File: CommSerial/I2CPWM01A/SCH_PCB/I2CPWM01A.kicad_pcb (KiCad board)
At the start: 2 copper layers, 30 x 40.1 mm, 45 parts, among them J1 CONN1_2, J10 JUMP2_2x1, J11 JUMP2_2x1, J12 JUMP2_2x1, J13 JUMP2_2x1, J14 JUMP_2x1, J15 JUMP_2x1, J16 JUMP_2x1, J17 JUMP_2x1, J18 JUMP_2x1, J19 JUMP_2x1, J2 CONN1_2, J20 JUMP_2x1, J21 JUMP_2x1, J3 JUMP_3X2, J4 JUMP_5X2, J5 JUMP_2x1, J6 JUMP2_2x1, J7 JUMP2_2x1, J8 JUMP2_2x1, J9 JUMP2_2x1, P1 _, P2 _, P3 _, P4 _, U1 PCA9531

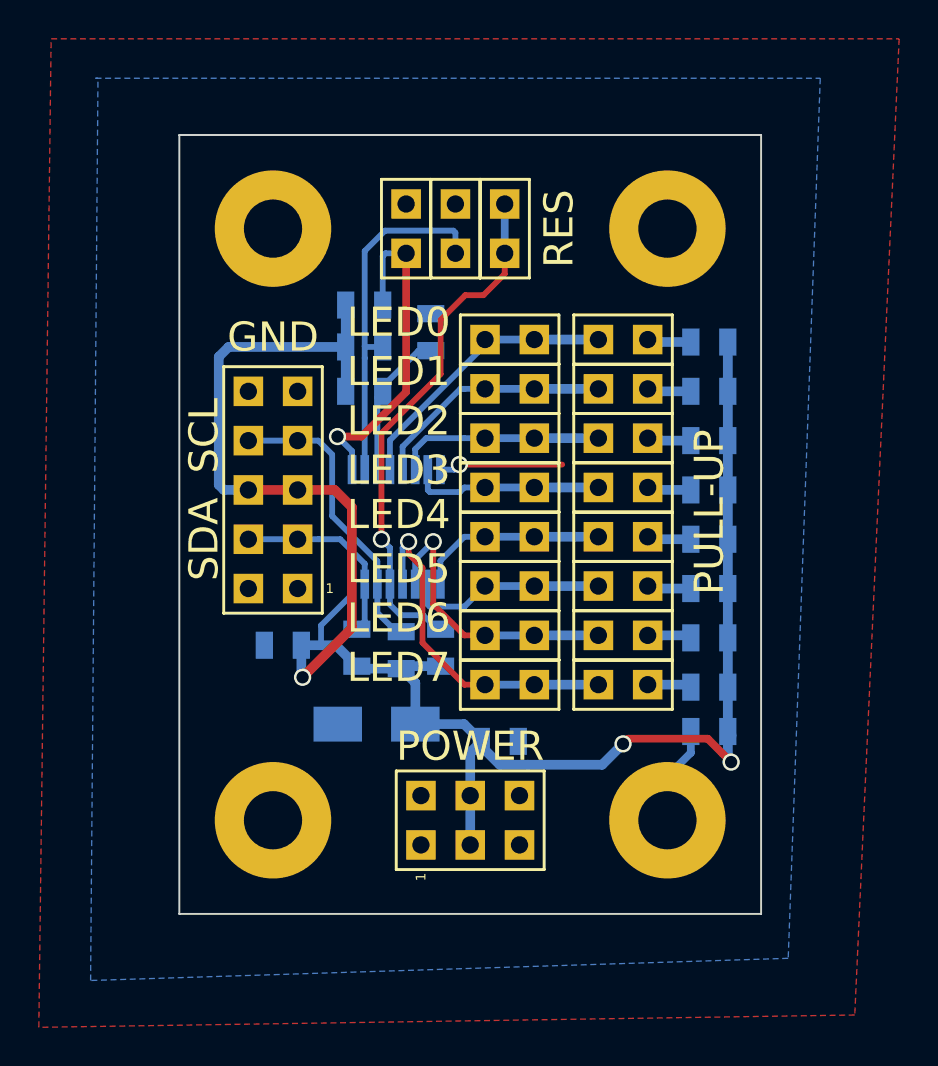
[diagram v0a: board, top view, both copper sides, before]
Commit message: 
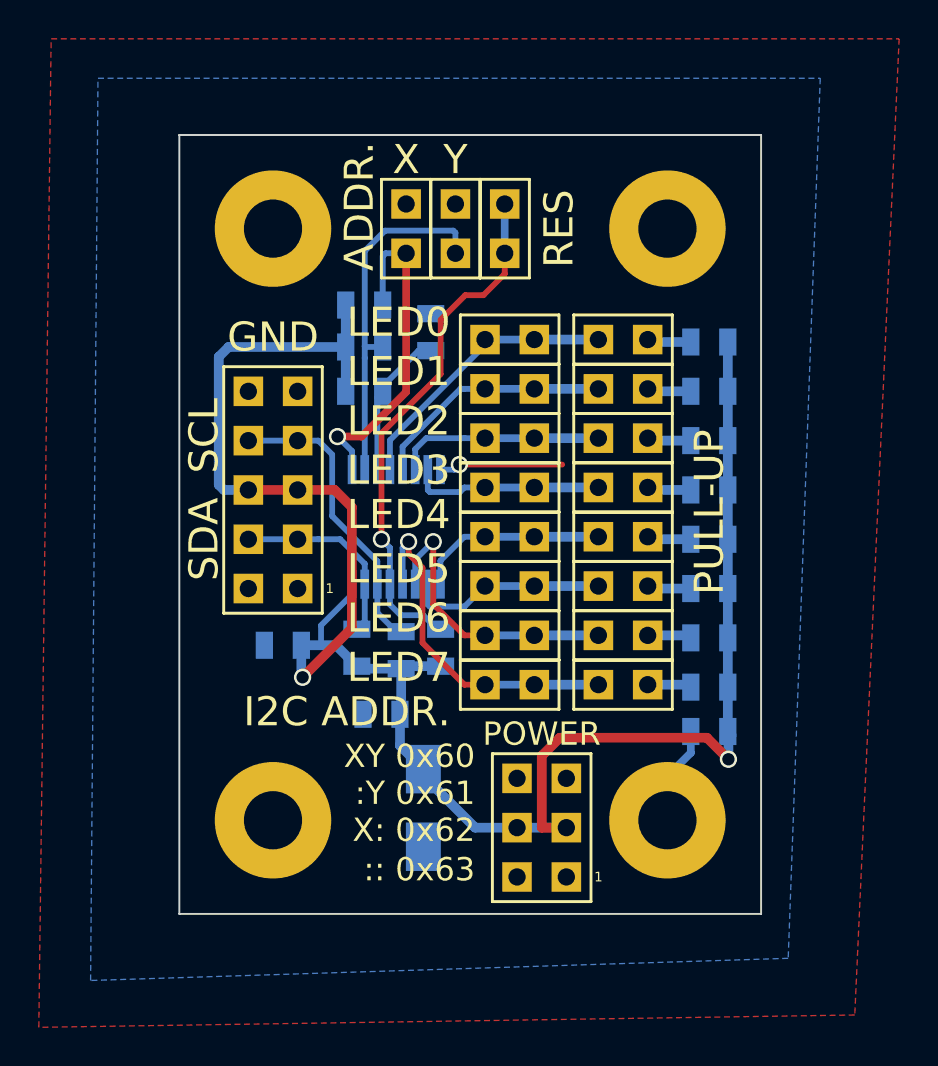
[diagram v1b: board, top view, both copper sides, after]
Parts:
- moved C3 6.25 mm to (10.7, -10.5), turned to 180 degrees
- moved D1 4.95 mm to (12.8, -5.71), turned to 90 degrees
- moved J3 3.70 mm to (18.9, -4.70), turned to 180 degrees
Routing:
- net VDD: track 97.2 -> 99.9 mm, vias 3 -> 2
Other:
- board text added: ":: 0x63"
- board text added: ":Y 0x61"
- board text added: "ADDR."
- board text added: "I2C ADDR."
- board text added: "X"
- board text added: "X: 0x62"
- board text added: "XY 0x60"
- board text added: "Y"

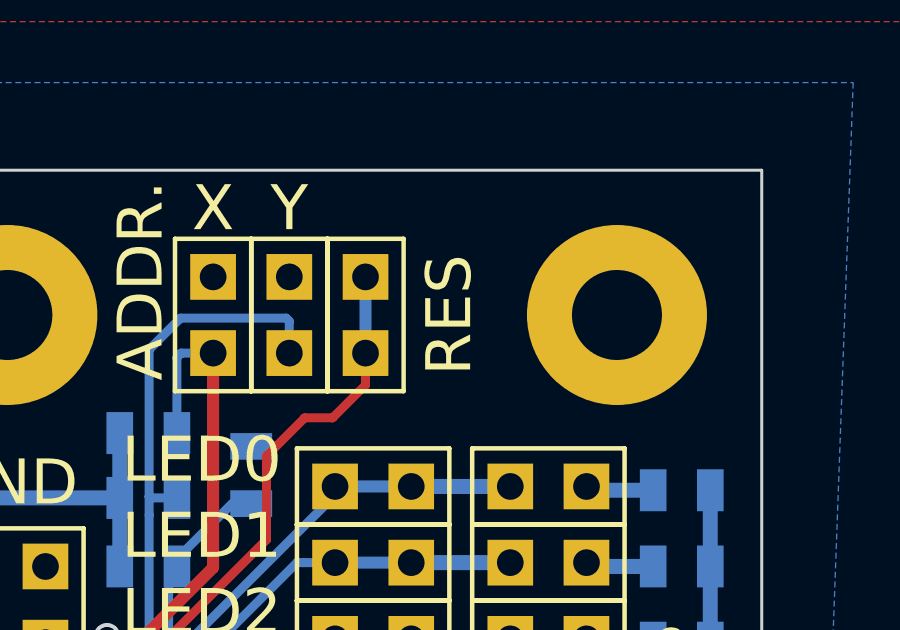
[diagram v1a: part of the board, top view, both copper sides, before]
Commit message: 
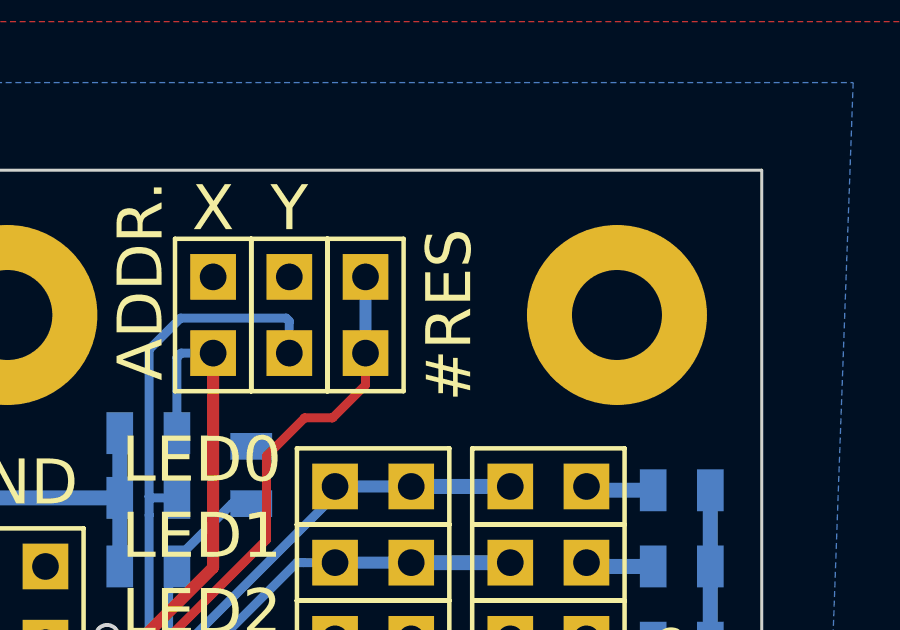
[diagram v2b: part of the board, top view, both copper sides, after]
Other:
- board text added: "#RES"
- board text removed: "RES"

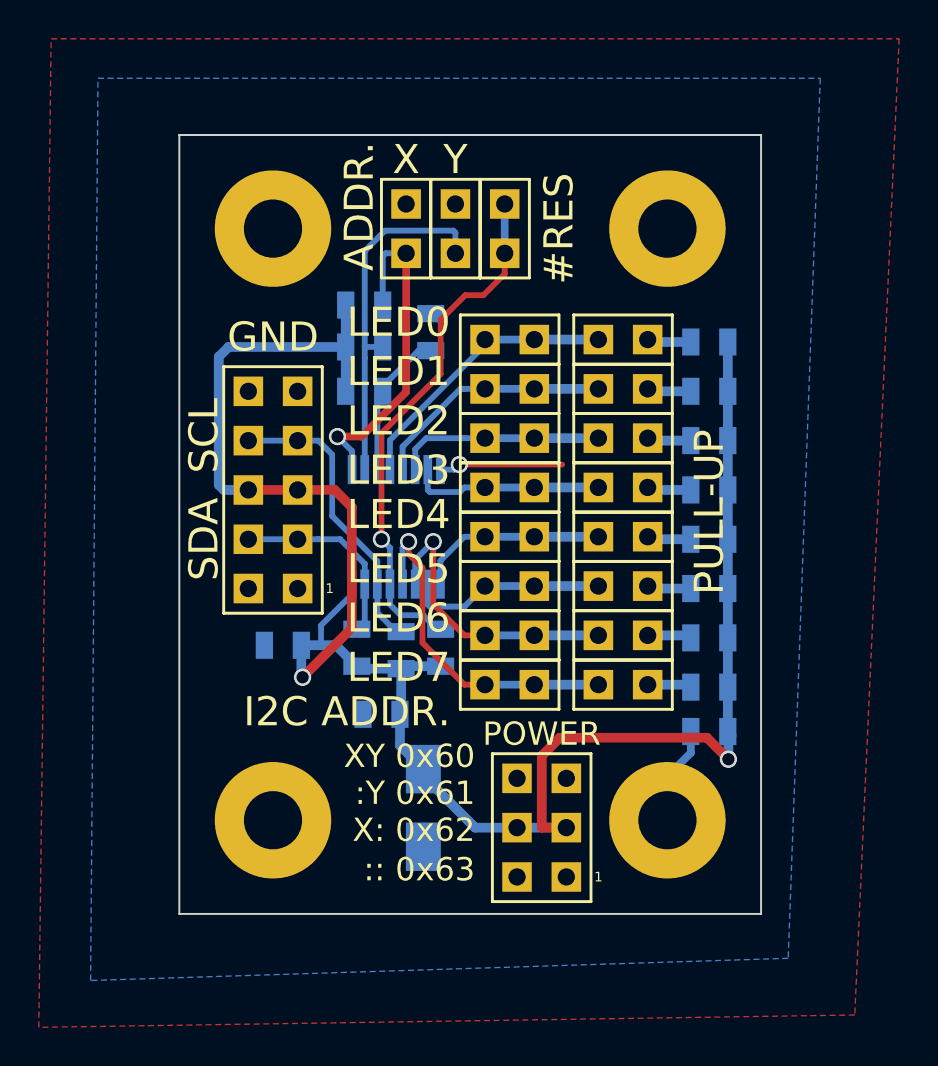
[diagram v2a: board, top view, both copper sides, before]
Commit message: upravy popisku a cest pro lepsi vedeni GND.
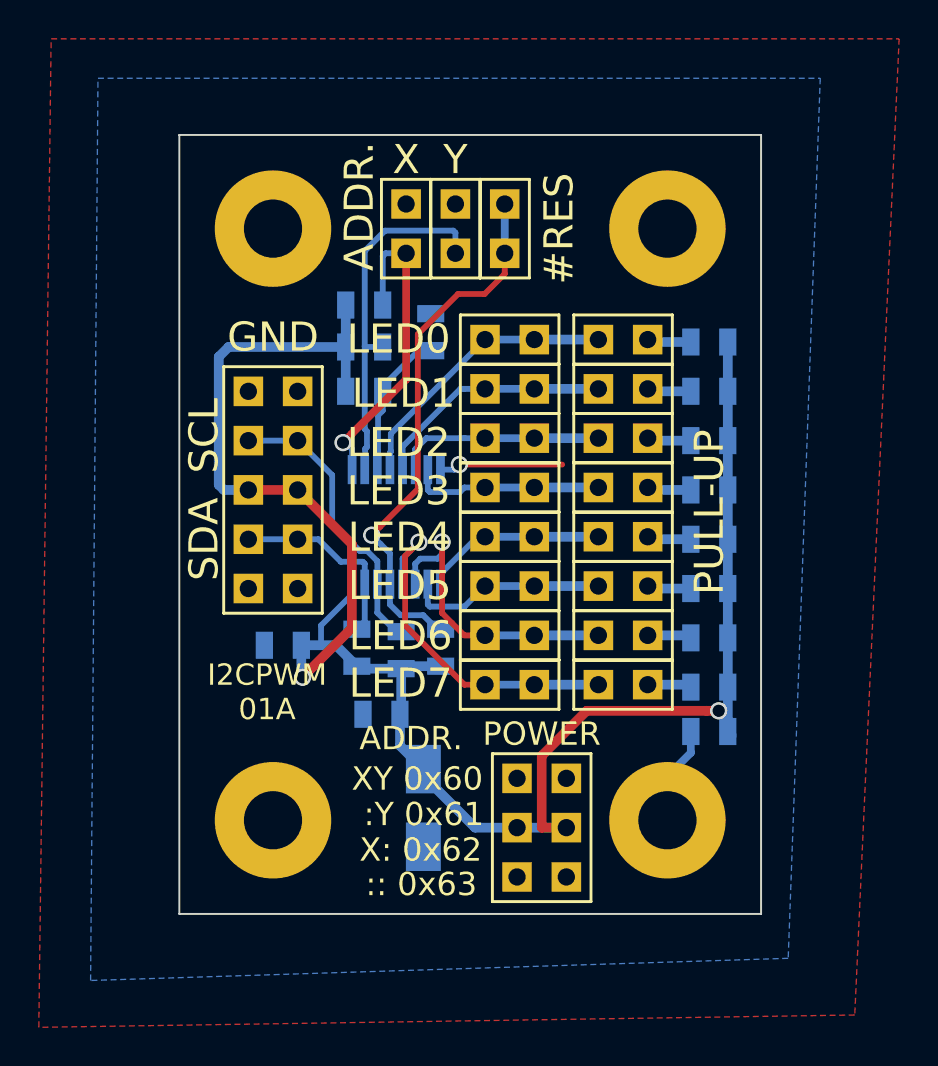
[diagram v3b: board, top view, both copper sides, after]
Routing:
- net VDD: track 99.9 -> 98.2 mm
- net /A0: track 17.4 -> 16.5 mm
- net Net-(J5-Pad1): track 27.1 -> 27.8 mm
- net /LED7: track 17.8 -> 18.3 mm
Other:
- board text added: "I2CPWM 01A"
- board text removed: "I2C ADDR."

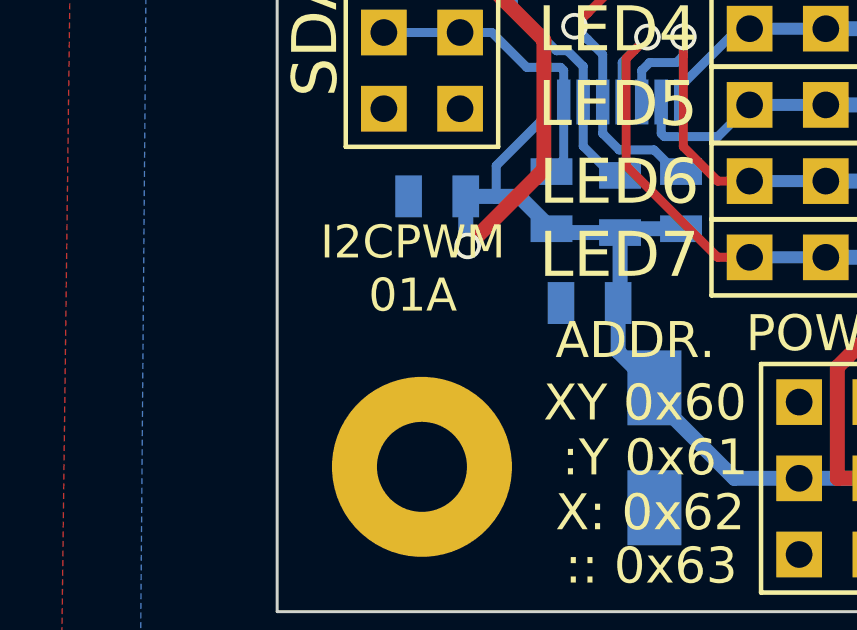
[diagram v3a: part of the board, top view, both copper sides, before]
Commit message: 
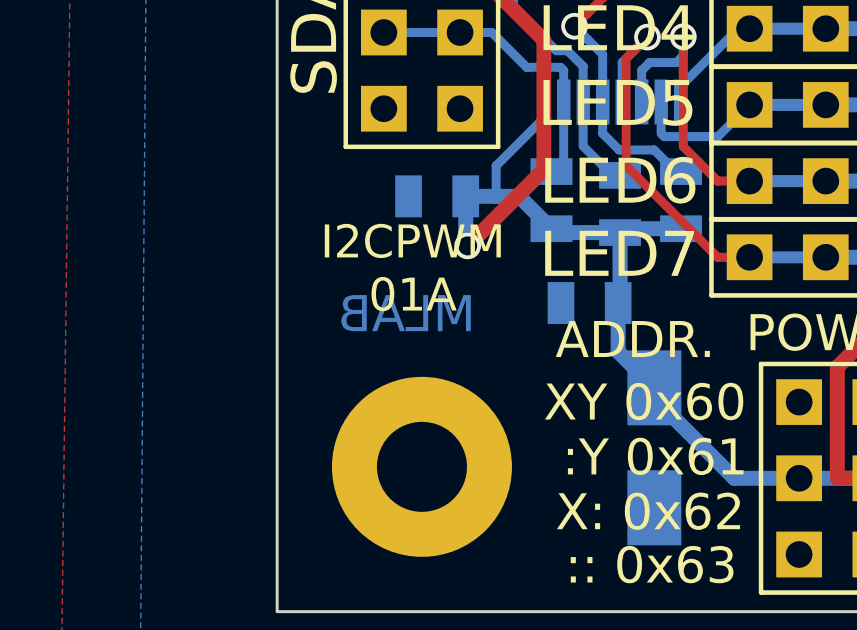
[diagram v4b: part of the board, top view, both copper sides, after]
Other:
- board text added: "MLAB"

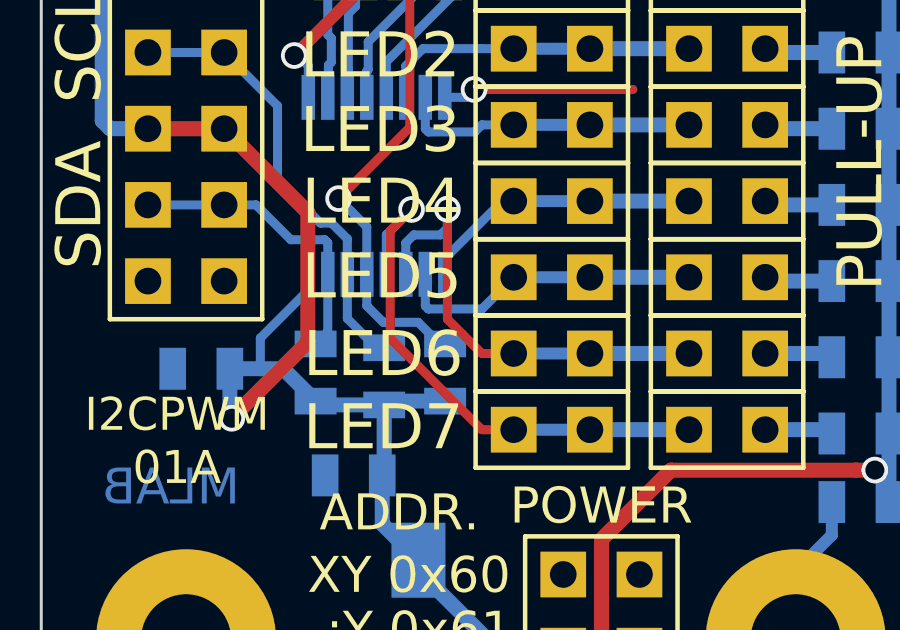
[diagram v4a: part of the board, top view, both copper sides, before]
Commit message: vygenerovani technologickych dat.
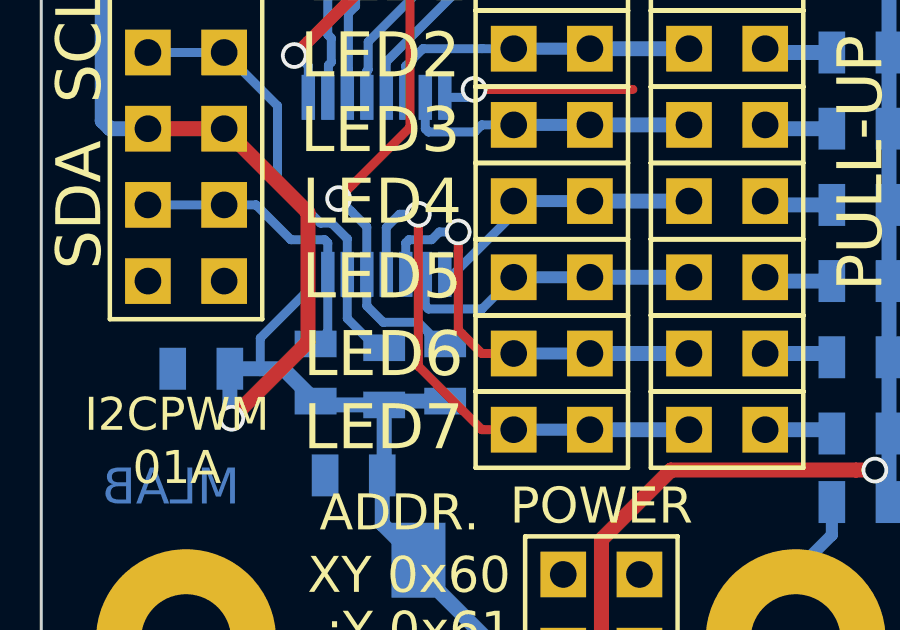
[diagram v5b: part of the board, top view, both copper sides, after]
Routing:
- net /LED6: track 15.5 -> 14.2 mm
- net /LED7: track 18.3 -> 17.8 mm

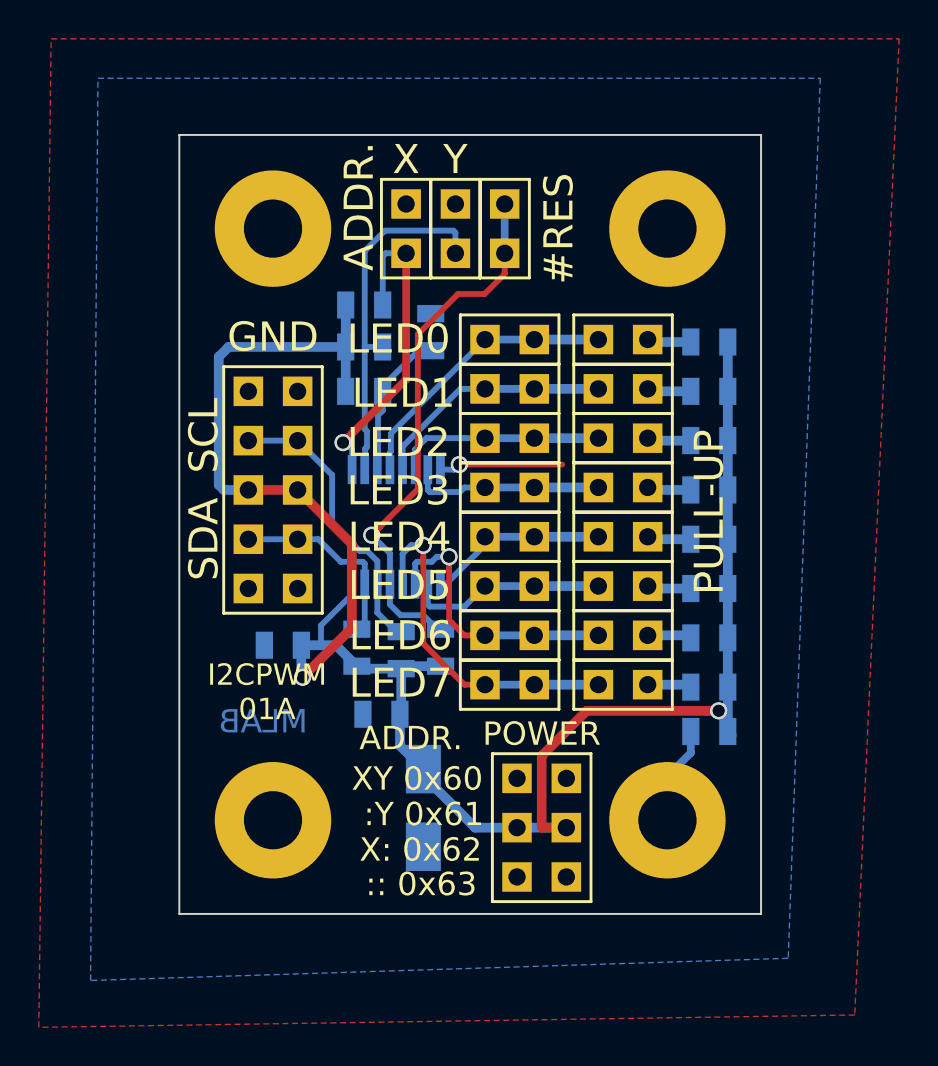
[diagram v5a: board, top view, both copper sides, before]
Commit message: 
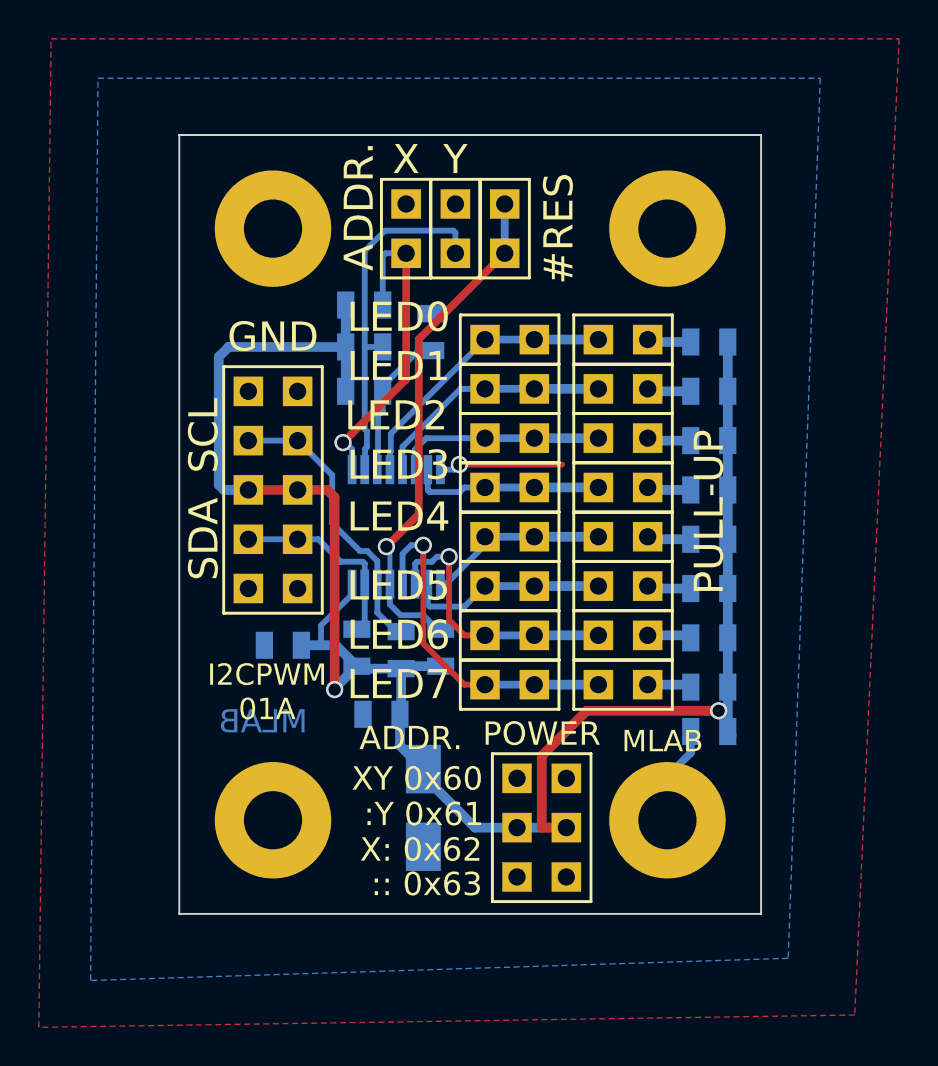
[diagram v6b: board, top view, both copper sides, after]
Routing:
- net Net-(J5-Pad1): track 27.8 -> 26.4 mm
